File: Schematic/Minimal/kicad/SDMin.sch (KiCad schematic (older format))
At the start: 79 parts

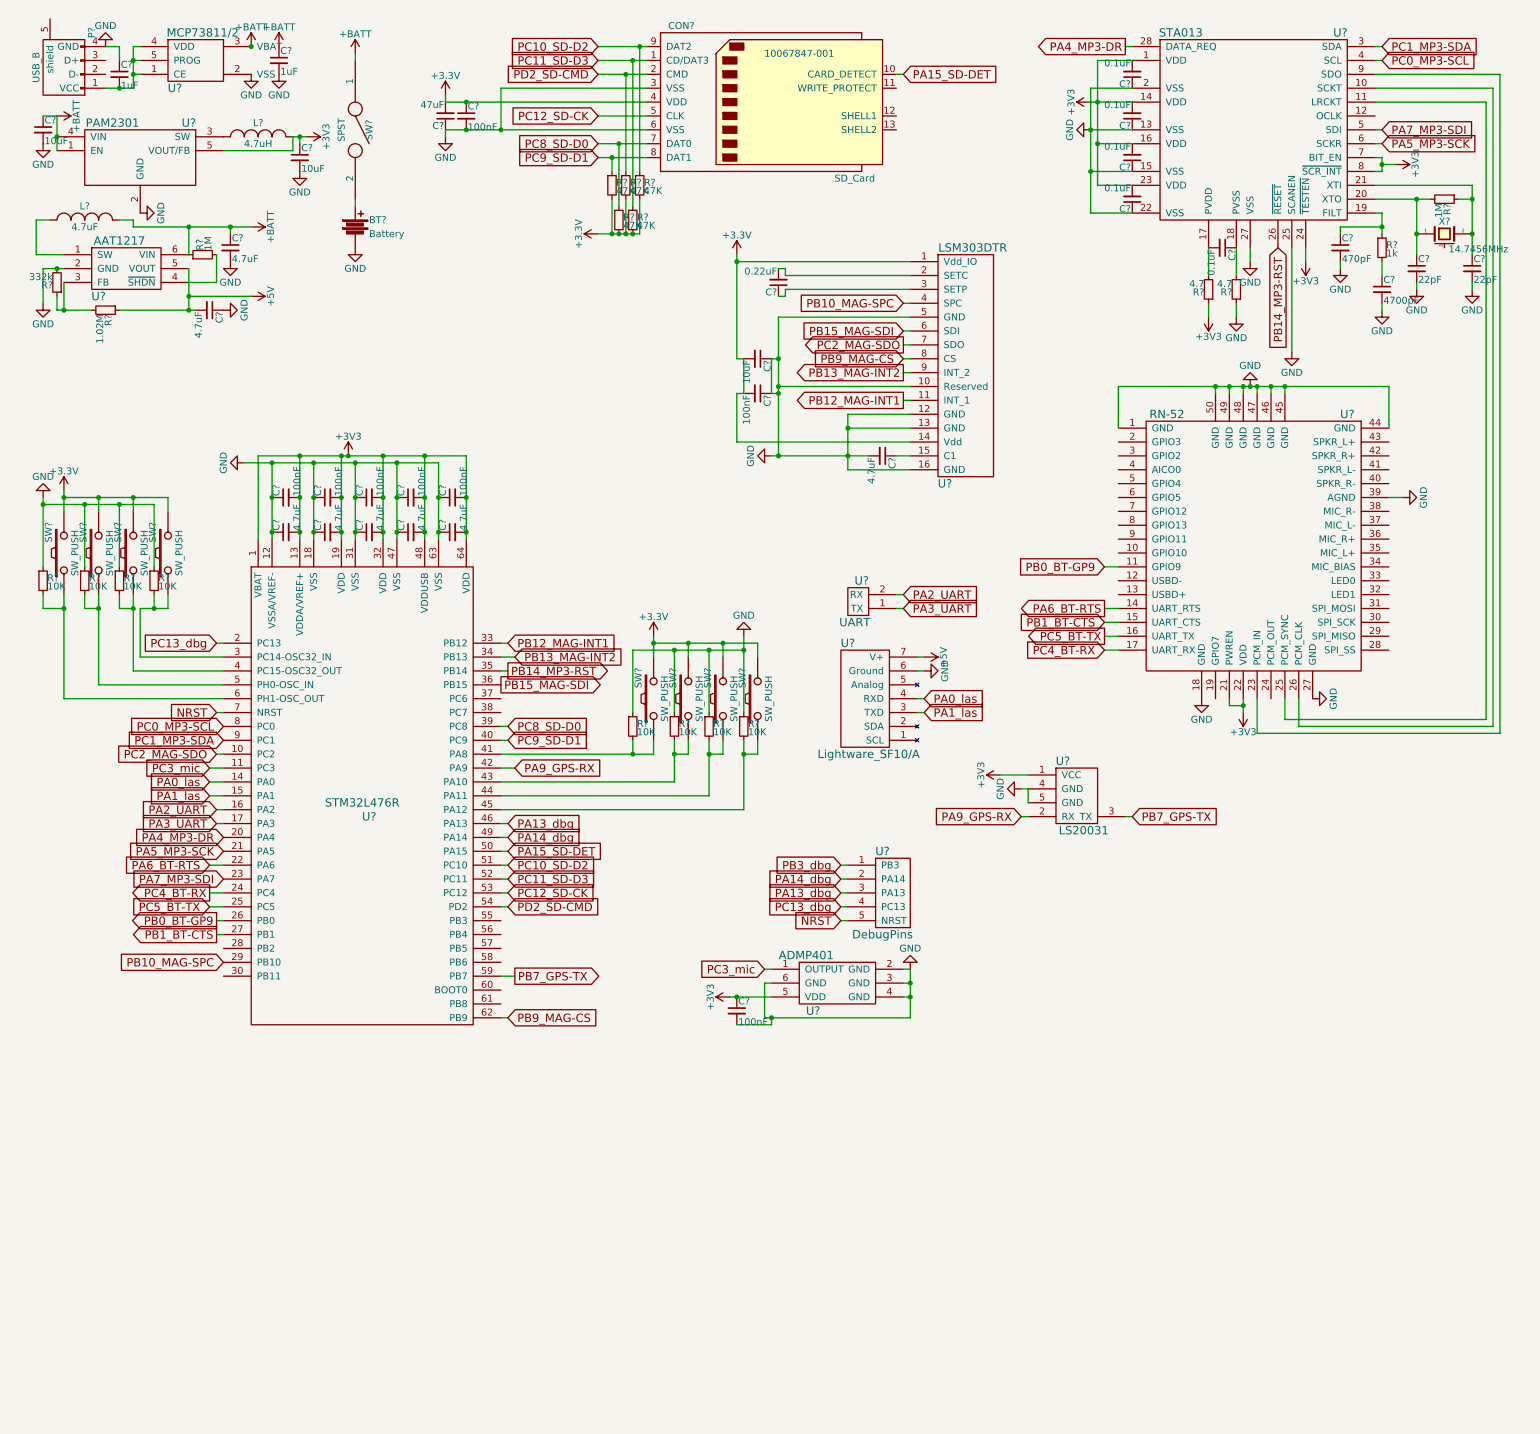
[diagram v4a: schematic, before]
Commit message: Update schematic (add software audio capability, prettier)
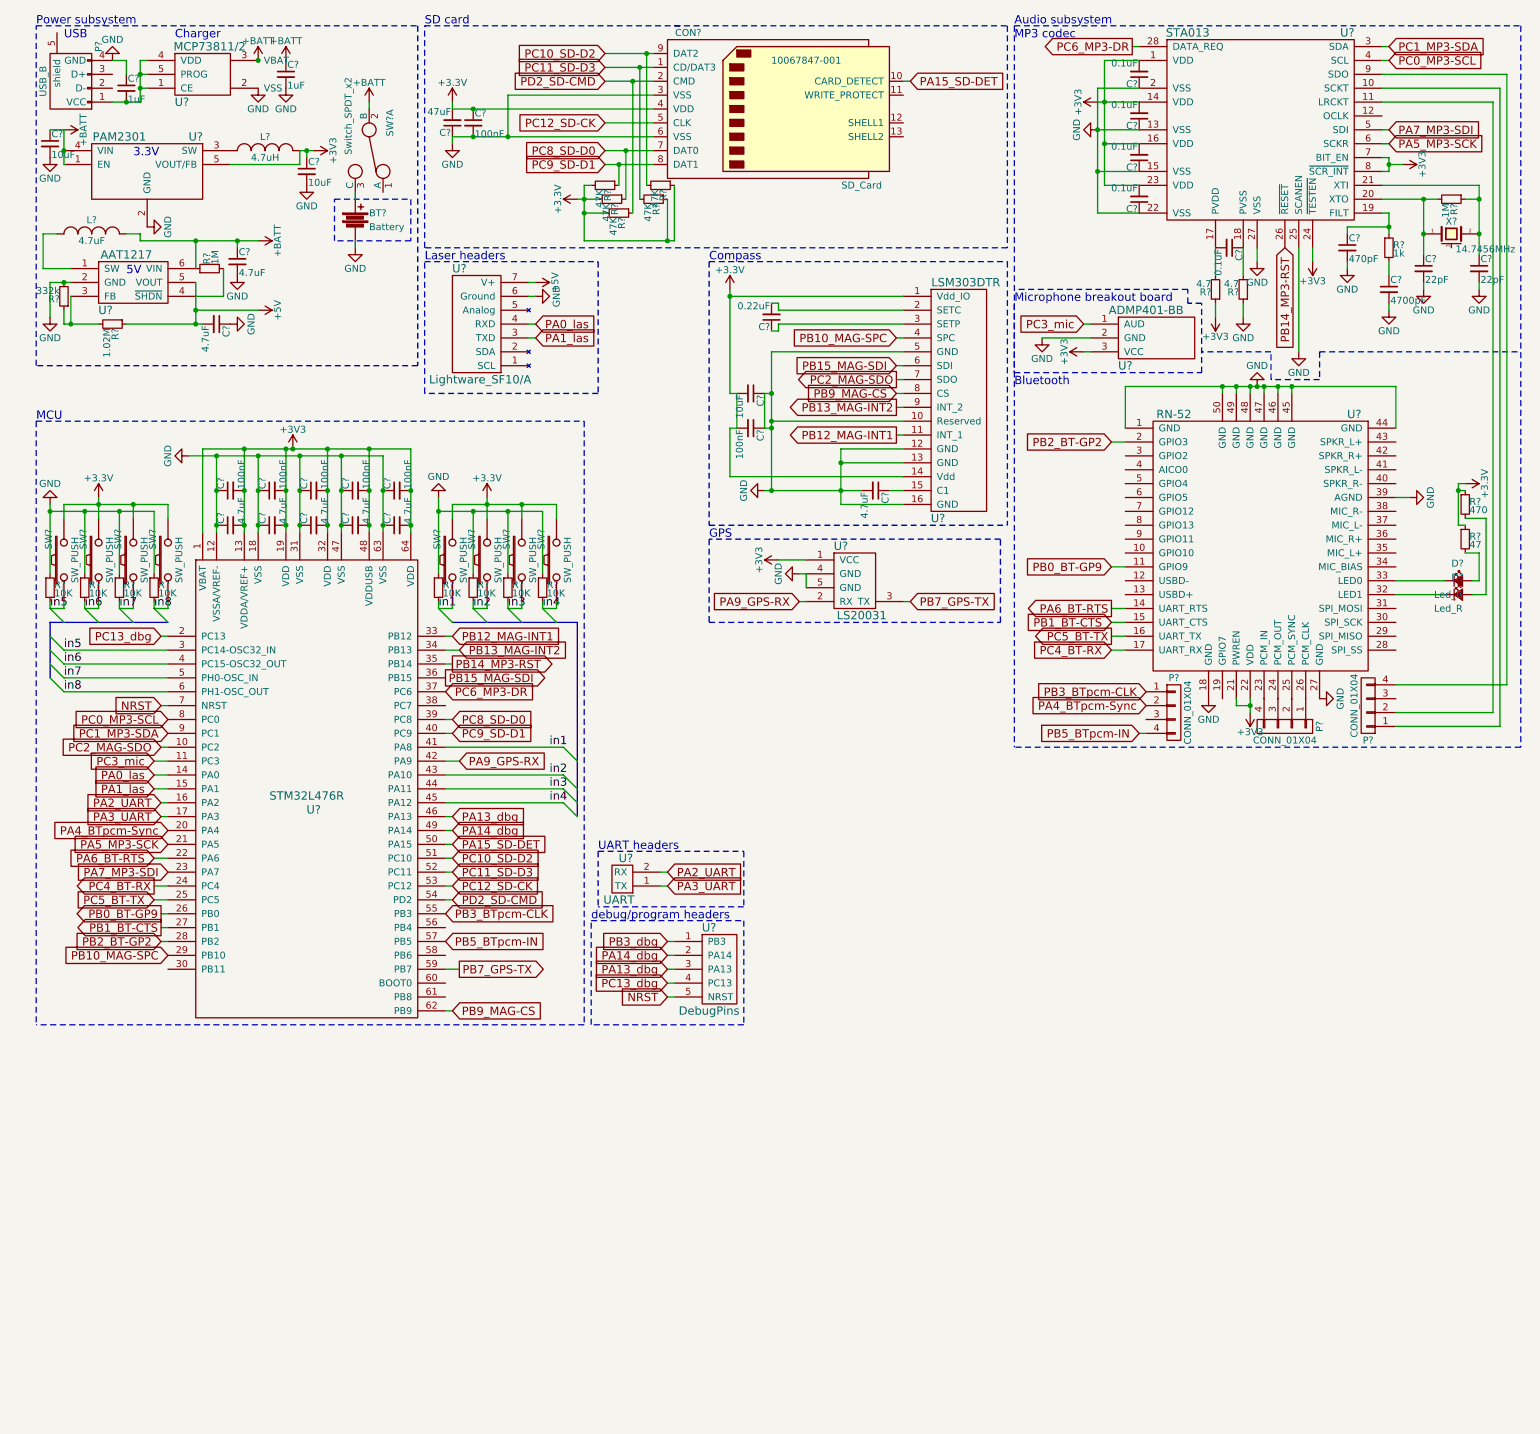
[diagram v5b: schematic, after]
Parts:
- removed C?: 100nF, symbol C_Small
- removed R? (x4): 10K, symbol R_Small
- removed SW? (x4): SW_PUSH, symbol SW_PUSH
- removed SW?: SPST, symbol SPST
- removed U?: ADMP401, symbol ADMP401
- added D?: Led_B, symbol Led_Small
- added D?: Led_R, symbol Led_Small
- added P? (x3): CONN_01X04, symbol CONN_01X04
- added R? (x4): 10K, symbol R_Small
- added R?: 470, symbol R_Small
- added R?: 47, symbol R_Small
- added SW? (x4): SW_PUSH, symbol SW_PUSH
- added SW?: Switch_SPDT_x2, symbol Switch_SPDT_x2
- added U?: ADMP401-BB, symbol ADMP401-BB
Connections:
- net +3V3: now also R?.1, R?.1, R?.1, R?.1, SW?.2, SW?.2, SW?.2, SW?.2, U?.3 (VCC); no longer R?.2, R?.2
- net +BATT: now also SW?.2 (B)
- net GND: now also R?.1, R?.1, R?.1, R?.1, U?.2 (GND)
- net PC10_SD-D2: now also R?.2; no longer R?.1
- net PC11_SD-D3: now also R?.2; no longer R?.1
- net PC3_mic: now also U?.1 (AUD)
- net PC8_SD-D0: now also R?.1; no longer R?.1
- net PC9_SD-D1: now also R?.1; no longer R?.1
- net PD2_SD-CMD: now also R?.1; no longer R?.1
- net PB2_BT-GP2: now reaches U?.28 (PB2)
- net PB2_BT-GP2: now also U?.2 (GPIO3)
- net in5: now reaches U?.3 (PC14-OSC32_IN)
- net in5: now also R?.2, SW?.1
- net PC6_MP3-DR: now reaches U?.37 (PC6)
- net PC6_MP3-DR: now also U?.28 (DATA_REQ)
- net in6: now reaches U?.4 (PC15-OSC32_OUT)
- net in6: now also R?.2, SW?.1
- net in1: now reaches R?.2, SW?.1, U?.41 (PA8)
- net in2: now reaches R?.2, SW?.1, U?.43 (PA10)
- net in3: now reaches R?.2, SW?.1, U?.44 (PA11)
- net in4: now reaches R?.2, SW?.1, U?.45 (PA12)
- net in7: now reaches U?.5 (PH0-OSC_IN)
- net in7: now also R?.2, SW?.1
- net PB3_BTpcm-CLK: now reaches U?.55 (PB3)
- net PB3_BTpcm-CLK: now also P?.1 (P1)
- net PB5_BTpcm-IN: now reaches U?.57 (PB5)
- net PB5_BTpcm-IN: now also P?.4 (P4)
- net in8: now reaches U?.6 (PH1-OSC_OUT)
- net in8: now also R?.2, SW?.1
- net at BT?.1: now also SW?.3 (C)
- net at U?.10 (SCKT): now also P?.1 (P1); no longer U?.26 (PCM_CLK)
- net at U?.11 (LRCKT): now also P?.2 (P2); no longer U?.25 (PCM_SYNC)
- net at U?.9 (SDO): now also P?.4 (P4); no longer U?.23 (PCM_IN)
- net at U?.24 (PCM_OUT): now also P?.3 (P3)
- net at U?.32 (LED1): now also D?.1 (K)
- net at U?.33 (LED0): now also D?.1 (K)
- net PA4_MP3-DR renamed PA4_BTpcm-Sync
- net PA4_BTpcm-Sync: now also P?.2 (P2); no longer U?.28 (DATA_REQ)
- new net: P?.4 (P4), U?.23 (PCM_IN)
- new net: P?.2 (P2), U?.25 (PCM_SYNC)
- new net: P?.1 (P1), U?.26 (PCM_CLK)
- new net: D?.2 (A), R?.2 (x2)
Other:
- note added: "3.3V"
- note added: "5V"
- note added: "Audio subsystem"
- note added: "Bluetooth"
- note added: "Charger"
- note added: "Compass"
- note added: "GPS"
- note added: "Laser headers"
- note added: "MCU"
- note added: "MP3 codec"
- note added: "Microphone breakout board"
- note added: "Power subsystem"
- note added: "SD card"
- note added: "UART headers"
- note added: "USB"
- note added: "debug/program headers"
- moved on the sheet: BT?, C?, CON?, L?, P?, R?, SW?, U?, X?

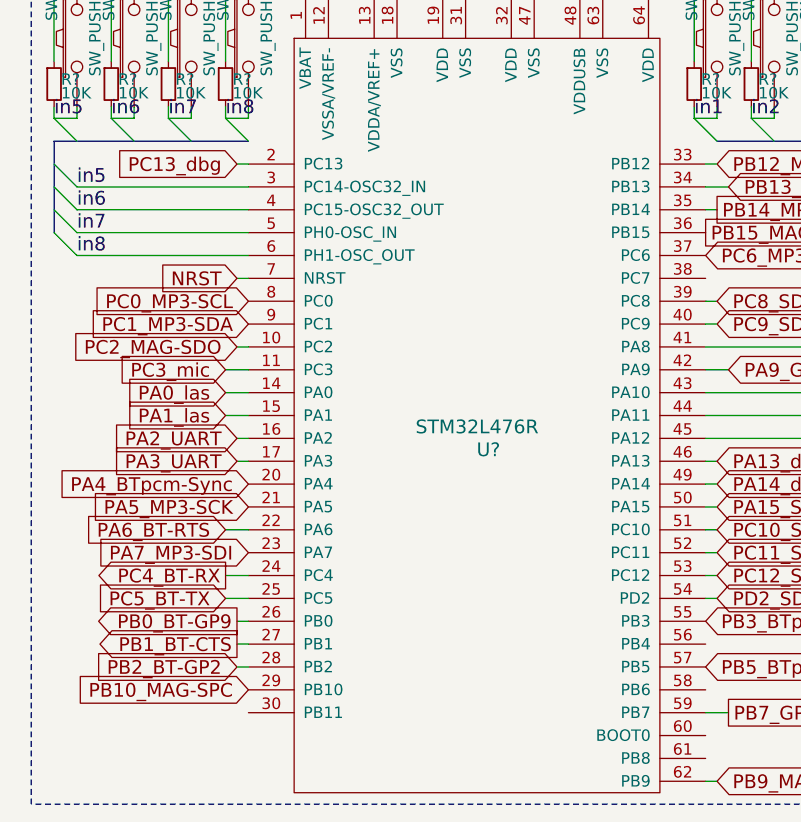
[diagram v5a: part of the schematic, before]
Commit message: sync (minor schematic change)
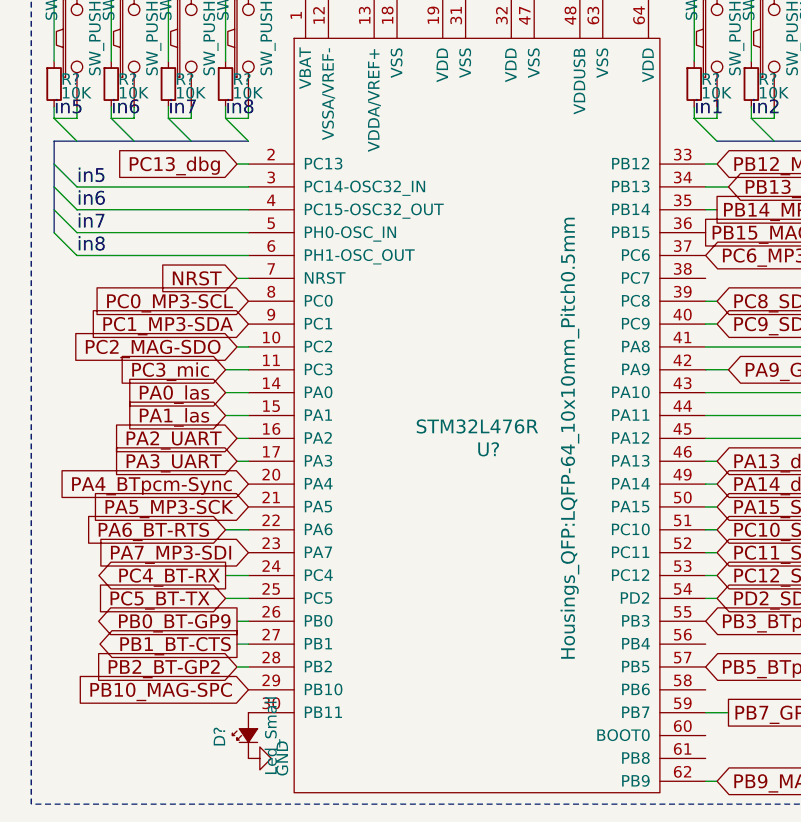
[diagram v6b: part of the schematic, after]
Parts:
- added D?: Led_Small, symbol Led_Small
- U?: footprint (none) -> Housings_QFP:LQFP-64_10x10mm_Pitch0.5mm
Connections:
- net GND: now also D?.1 (K)
- net at U?.30 (PB11): now also D?.2 (A)
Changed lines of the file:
@@
 F 0 "U?" H 2500 6100 60  0000 C CNN
 F 1 "STM32L476R" H 2450 6200 60  0000 C CNN
-F 2 "" H 2150 6150 60  0000 C CNN
+F 2 "Housings_QFP:LQFP-64_10x10mm_Pitch0.5mm" V 2850 6150 60  0000 C CNN
 F 3 "" H 2150 6150 60  0000 C CNN
 	1    2450 6150
@@
 Wire Notes Line
 	2650 2100 2650 1800
+$Comp
+L Led_Small D?
+U 1 1 56D3567B
+P 1450 7450
+F 0 "D?" H 1400 7575 50  0000 L CNN
+F 1 "Led_Small" H 1275 7350 50  0000 L CNN
+F 2 "" V 1450 7450 50  0000 C CNN
+F 3 "" V 1450 7450 50  0000 C CNN
+	1    1450 7450
+	0    -1   -1   0
+$EndComp
+$Comp
+L GND #PWR?
+U 1 1 56D358B6
+P 1450 7550
+F 0 "#PWR?" H 1450 7300 50  0001 C CNN
+F 1 "GND" H 1450 7400 50  0000 C CNN
+F 2 "" H 1450 7550 50  0000 C CNN
+F 3 "" H 1450 7550 50  0000 C CNN
+	1    1450 7550
+	0    -1   -1   0
+$EndComp
 $EndSCHEMATC
